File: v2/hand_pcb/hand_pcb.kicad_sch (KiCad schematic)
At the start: 50 parts, among them J1 Screw_Terminal_01x10, J10 8P8C, J2 Conn_01x08, J3 Conn_01x08, J4 Conn_01x02, J5 Conn_01x02, J9 Conn_02x02_Top_Bottom, M1 Motor_Servo_FB, M10 Motor_Servo_FB, M2 Motor_Servo_FB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

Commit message: Added hand ADCs
Subject to change without notice
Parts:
- added R22, R23, R24, R25, R26, R27, R28, R29: 0R, Resistor_THT:R_Axial_DIN0207_L6.3mm_D2.5mm_P10.16mm_Horizontal, symbol Device:R_US
- added U4, U5: ADS7830, Package_SO:TSSOP-16_4.4x5mm_P0.65mm, symbol Analog_DAC:ADS7830
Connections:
- net +5V: now also R22.2, R25.1, R27.1, R29.2, U4.10 (REFin/REFout), U4.16 (VDD), U5.10 (REFin/REFout), U5.16 (VDD)
- net GND: now also R23.2, R24.1, R26.1, R28.2, U4.11 (COM), U4.9 (GND), U5.11 (COM), U5.9 (GND)
- net SCL: now also U4.14 (SCL), U5.14 (SCL)
- net SDA: now also U4.15 (SDA), U5.15 (SDA)
- net SERVO_FB_1: now also U4.1 (CH0)
- net SERVO_FB_10: now also U5.2 (CH1)
- net SERVO_FB_2: now also U4.2 (CH1)
- net SERVO_FB_3: now also U4.3 (CH2)
- net SERVO_FB_4: now also U4.4 (CH3)
- net SERVO_FB_5: now also U4.5 (CH4)
- net SERVO_FB_6: now also U4.6 (CH5)
- net SERVO_FB_7: now also U4.7 (CH6)
- net SERVO_FB_8: now also U4.8 (CH7)
- net SERVO_FB_9: now also U5.1 (CH0)
- new net: R28.1, R29.1, U5.12 (A0)
- new net: R26.2, R27.2, U5.13 (A1)
- new net: R22.1, R23.1, U4.12 (A0)
- new net: R24.2, R25.2, U4.13 (A1)
- no-connect marks 18 -> 24
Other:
- moved on the sheet: D6, D7, J4, J5, R10, R11, R20, R21

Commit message: Doing stuff
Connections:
- net SERVO_FB_1: now also U4.8 (CH7); no longer U4.1 (CH0)
- net SERVO_FB_10: now also U5.1 (CH0); no longer U5.2 (CH1)
- net SERVO_FB_2: now also U4.7 (CH6); no longer U4.2 (CH1)
- net SERVO_FB_3: now also U4.6 (CH5); no longer U4.3 (CH2)
- net SERVO_FB_4: now also U4.5 (CH4); no longer U4.4 (CH3)
- net SERVO_FB_5: now also U4.4 (CH3); no longer U4.5 (CH4)
- net SERVO_FB_6: now also U4.3 (CH2); no longer U4.6 (CH5)
- net SERVO_FB_7: now also U4.2 (CH1); no longer U4.7 (CH6)
- net SERVO_FB_8: now also U4.1 (CH0); no longer U4.8 (CH7)
- net SERVO_FB_9: now also U5.2 (CH1); no longer U5.1 (CH0)

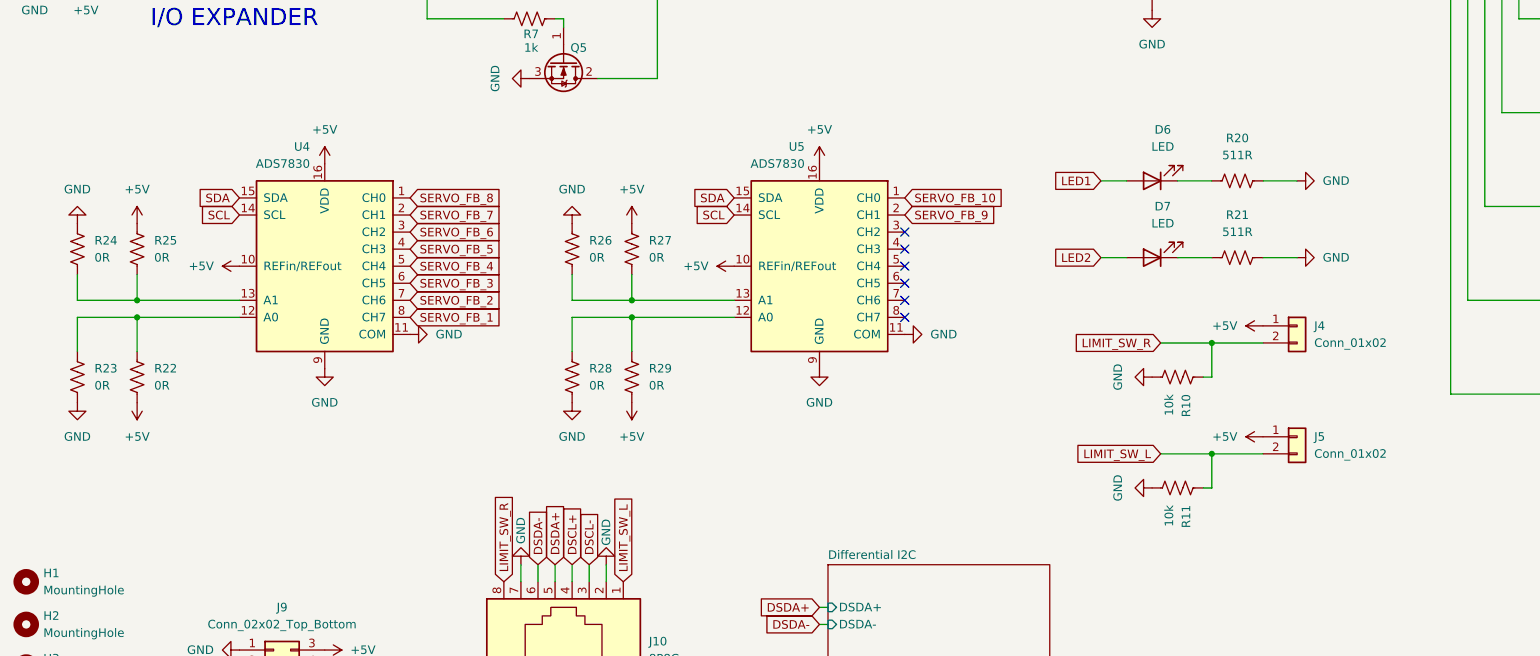
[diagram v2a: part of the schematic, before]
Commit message: Replaced hand ADCs with ADS7138
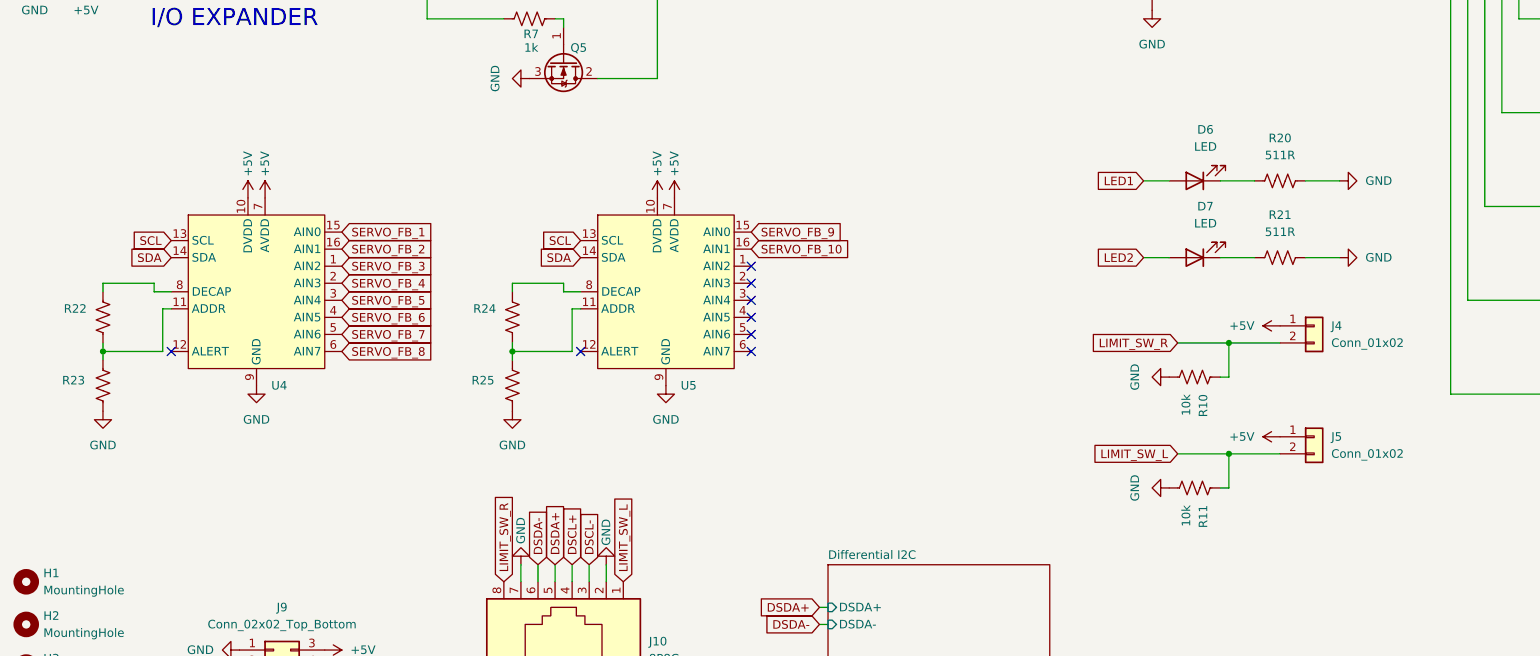
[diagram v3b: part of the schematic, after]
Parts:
- removed R26, R27, R28, R29: 0R, Resistor_THT:R_Axial_DIN0207_L6.3mm_D2.5mm_P10.16mm_Horizontal, symbol Device:R_US
- removed U4, U5: ADS7830, Package_SO:TSSOP-16_4.4x5mm_P0.65mm, symbol Analog_DAC:ADS7830
- added U4, U5: ~, Package_DFN_QFN:WQFN-16-1EP_3x3mm_P0.5mm_EP1.68x1.68mm, symbol bh_symbol_library:ADS7138IRTER
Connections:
- net +5V: now also U4.10 (DVDD), U4.7 (AVDD), U5.10 (DVDD), U5.7 (AVDD); no longer R22.2, R25.1
- net GND: now also R25.2, U4.9 (GND), U5.9 (GND); no longer R24.1
- net SCL: now also U4.13 (SCL), U5.13 (SCL)
- net SDA: now also U4.14 (SDA), U5.14 (SDA)
- net SERVO_FB_1: now also U4.15 (AIN0)
- net SERVO_FB_10: now also U5.16 (AIN1)
- net SERVO_FB_2: now also U4.16 (AIN1)
- net SERVO_FB_3: now also U4.1 (AIN2)
- net SERVO_FB_4: now also U4.2 (AIN3)
- net SERVO_FB_5: now also U4.3 (AIN4)
- net SERVO_FB_6: now also U4.4 (AIN5)
- net SERVO_FB_7: now also U4.5 (AIN6)
- net SERVO_FB_8: now also U4.6 (AIN7)
- net SERVO_FB_9: now also U5.15 (AIN0)
- net at R23.1: now also R22.2, U4.11 (ADDR); no longer R22.1
- net at R24.2: now also R25.1, U5.11 (ADDR); no longer R25.2
- new net: R22.1, U4.8 (DECAP)
- new net: R24.1, U5.8 (DECAP)
- no-connect marks 24 -> 26
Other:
- moved on the sheet: D6, D7, J4, J5, R10, R11, R20, R21

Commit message: Doing some things
Crossing some ts and dotting some is. Making v3 of the BOM.
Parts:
- D1, D2, D3, D4, D5: value 1N5819 -> SB5100-T; footprint Diode_THT:D_DO-41_SOD81_P10.16mm_Horizontal -> Diode_THT:D_DO-201AD_P12.70mm_Horizontal; Digikey (none) -> https://www.digikey.ca/en/products/detail/diodes-incorporat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
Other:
- moved on the sheet: R22, R23, R24, R25, U4, U5

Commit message: Doing some things
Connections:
- net SERVO_FB_1: now also U4.6 (AIN7); no longer U4.15 (AIN0)
- net SERVO_FB_10: now also U5.15 (AIN0); no longer U5.16 (AIN1)
- net SERVO_FB_2: now also U4.5 (AIN6); no longer U4.16 (AIN1)
- net SERVO_FB_3: now also U4.4 (AIN5); no longer U4.1 (AIN2)
- net SERVO_FB_4: now also U4.3 (AIN4); no longer U4.2 (AIN3)
- net SERVO_FB_5: now also U4.2 (AIN3); no longer U4.3 (AIN4)
- net SERVO_FB_6: now also U4.1 (AIN2); no longer U4.4 (AIN5)
- net SERVO_FB_7: now also U4.16 (AIN1); no longer U4.5 (AIN6)
- net SERVO_FB_8: now also U4.15 (AIN0); no longer U4.6 (AIN7)
- net SERVO_FB_9: now also U5.16 (AIN1); no longer U5.15 (AIN0)

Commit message: Doing more things
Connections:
- net +12V: now also J9.3 (Pin_3); no longer J9.4 (Pin_4)
- net +5V: now also J9.4 (Pin_4); no longer J9.3 (Pin_3)
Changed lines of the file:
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@@
 	(wire
 		(pts
-			(xy 30.48 52.07) (xy 31.75 52.07)
-		)
-		(stroke
-			(width 0)
-			(type default)
-		)
-	)
-	(wire
-		(pts
 			(xy 121.92 67.31) (xy 121.92 69.85)
 		)
@@
 	(wire
 		(pts
-			(xy 30.48 53.34) (xy 30.48 52.07)
-		)
-		(stroke
-			(width 0)
-			(type default)
-		)
-	)
-	(wire
-		(pts
 			(xy 224.79 34.29) (xy 222.25 34.29)
 		)
@@
 	(symbol
 		(lib_id "power:+12V")
-		(at 63.5 184.15 270)
+		(at 63.5 181.61 270)
 		(unit 1)
 		(exclude_from_sim no)
@@
 		(fields_autoplaced yes)
 		(property "Reference" "#PWR065"
-			(at 59.69 184.15 0)
+			(at 59.69 181.61 0)
 			(effects
 				(font
@@
 		)
 		(property "Value" "+12V"
-			(at 67.31 184.1499 90)
+			(at 67.31 181.6099 90)
 			(effects
 				(font
@@
 		)
 		(property "Footprint" ""
-			(at 63.5 184.15 0)
+			(at 63.5 181.61 0)
 			(effects
 				(font
@@
 		)
 		(property "Datasheet" ""
-			(at 63.5 184.15 0)
+			(at 63.5 181.61 0)
 			(effects
 				(font
@@
 		)
 		(property "Description" "Power symbol creates a global label with name \"+12V\""
-			(at 63.5 184.15 0)
+			(at 63.5 181.61 0)
 			(effects
 				(font
@@
 	(symbol
 		(lib_id "power:+5V")
-		(at 30.48 53.34 180)
+		(at 31.75 52.07 90)
 		(unit 1)
 		(exclude_from_sim no)
@@
 		(on_board yes)
 		(dnp no)
-		(fields_autoplaced yes)
 		(property "Reference" "#PWR06"
-			(at 30.48 49.53 0)
+			(at 35.56 52.07 0)
 			(effects
 				(font
@@
 		)
 		(property "Value" "+5V"
-			(at 30.48 58.42 0)
+			(at 30.48 54.102 90)
 			(effects
 				(font
@@
 		)
 		(property "Footprint" ""
-			(at 30.48 53.34 0)
+			(at 31.75 52.07 0)
 			(effects
 				(font
@@
 		)
 		(property "Datasheet" ""
-			(at 30.48 53.34 0)
+			(at 31.75 52.07 0)
 			(effects
 				(font
@@
 		)
 		(property "Description" "Power symbol creates a global label with name \"+5V\""
-			(at 30.48 53.34 0)
+			(at 31.75 52.07 0)
 			(effects
 				(font
@@
 	(symbol
 		(lib_id "power:+5V")
-		(at 63.5 181.61 270)
+		(at 63.5 184.15 270)
 		(unit 1)
 		(exclude_from_sim no)
@@
 		(fields_autoplaced yes)
 		(property "Reference" "#PWR067"
-			(at 59.69 181.61 0)
+			(at 59.69 184.15 0)
 			(effects
 				(font
@@
 		)
 		(property "Value" "+5V"
-			(at 67.31 181.6099 90)
+			(at 67.31 184.1499 90)
 			(effects
 				(font
@@
 		)
 		(property "Footprint" ""
-			(at 63.5 181.61 0)
+			(at 63.5 184.15 0)
 			(effects
 				(font
@@
 		)
 		(property "Datasheet" ""
-			(at 63.5 181.61 0)
+			(at 63.5 184.15 0)
 			(effects
 				(font
@@
 		)
 		(property "Description" "Power symbol creates a global label with name \"+5V\""
-			(at 63.5 181.61 0)
+			(at 63.5 184.15 0)
 			(effects
 				(font
